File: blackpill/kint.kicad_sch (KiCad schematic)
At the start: 19 parts, among them J1 THUMB_RIGHT_SPC_KB600, J2 LEFT_13_LT, J3 TOP_LEFT, J4 TOP_RIGHT, J5 THUMB_LEFT_BAK, J6 THUMB_RIGHT_SPC, J7 RIGHT_13_DOWN, J8 THUMB_LEFT_BAK_KB600, U1 YAAJ_WeAct_BlackPill_Part_Lik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

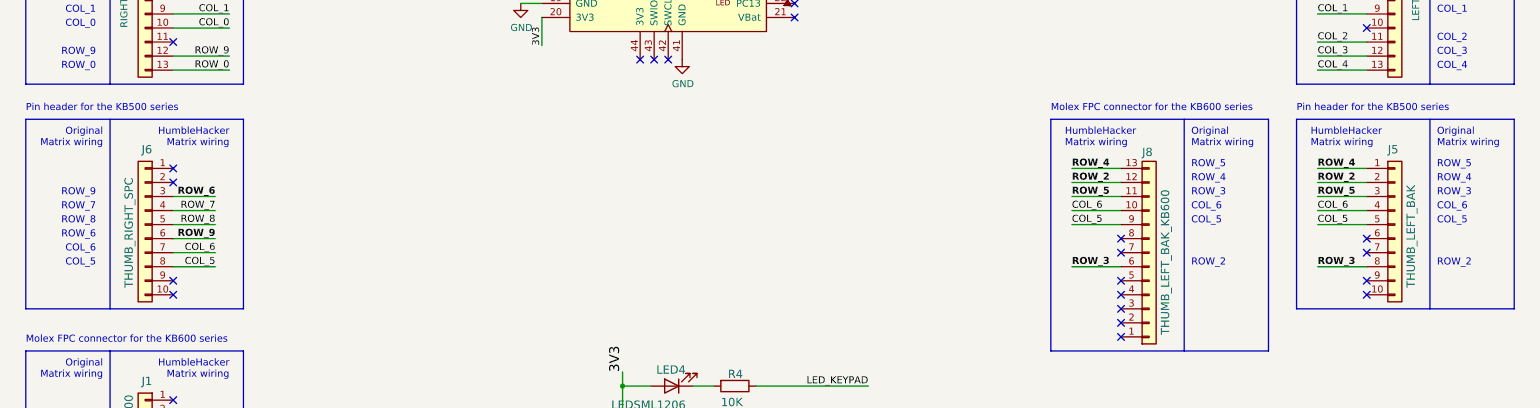
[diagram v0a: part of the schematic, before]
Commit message: remove unused KB500 connectors and move components
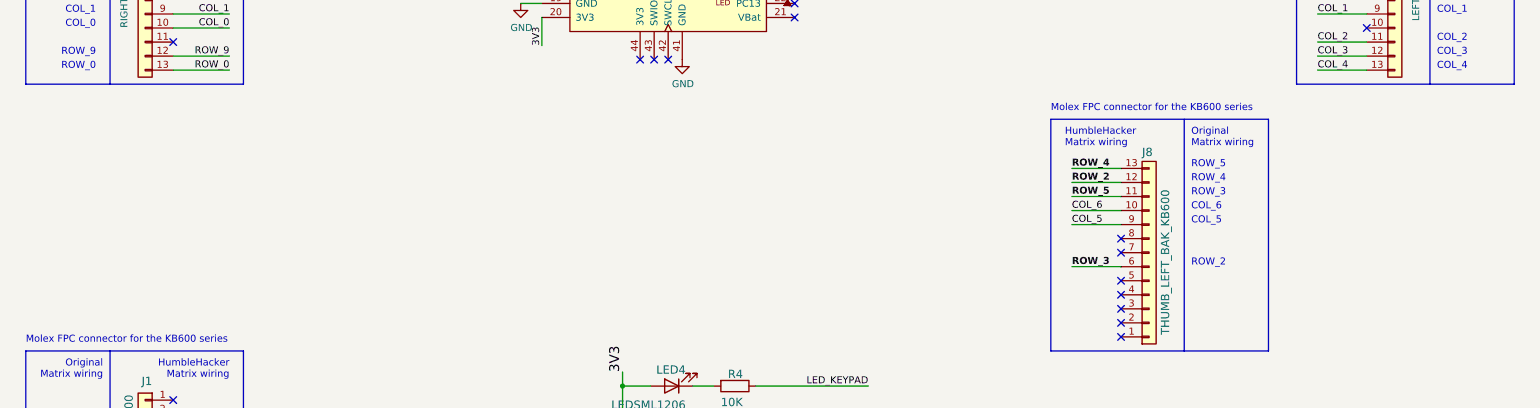
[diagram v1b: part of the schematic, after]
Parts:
- removed J5: THUMB_LEFT_BAK, Connector_PinHeader_2.54mm:PinHeader_1x10_P2.54mm_Vertical, symbol Connector_Generic:Conn_01x10
- removed J6: THUMB_RIGHT_SPC, Connector_PinHeader_2.54mm:PinHeader_1x10_P2.54mm_Vertical, symbol Connector_Generic:Conn_01x10
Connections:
- no-connect marks 45 -> 37
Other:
- note removed: "Pin header for the KB500 series"
